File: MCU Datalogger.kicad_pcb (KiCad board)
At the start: 2 copper layers, 50.8 x 31.9 mm, 30 parts, among them J1 Conn_01x04_Pin, J2 Conn_01x04_Pin, J3 Conn_01x09_Pin, J4 Conn_02x03_Odd_Even, U1 24LC1025, U2 24LC1025, U3 ATMEGA328P-AU, U4 DS1337S_, Y1 32.768kHz, Y2 16KHz

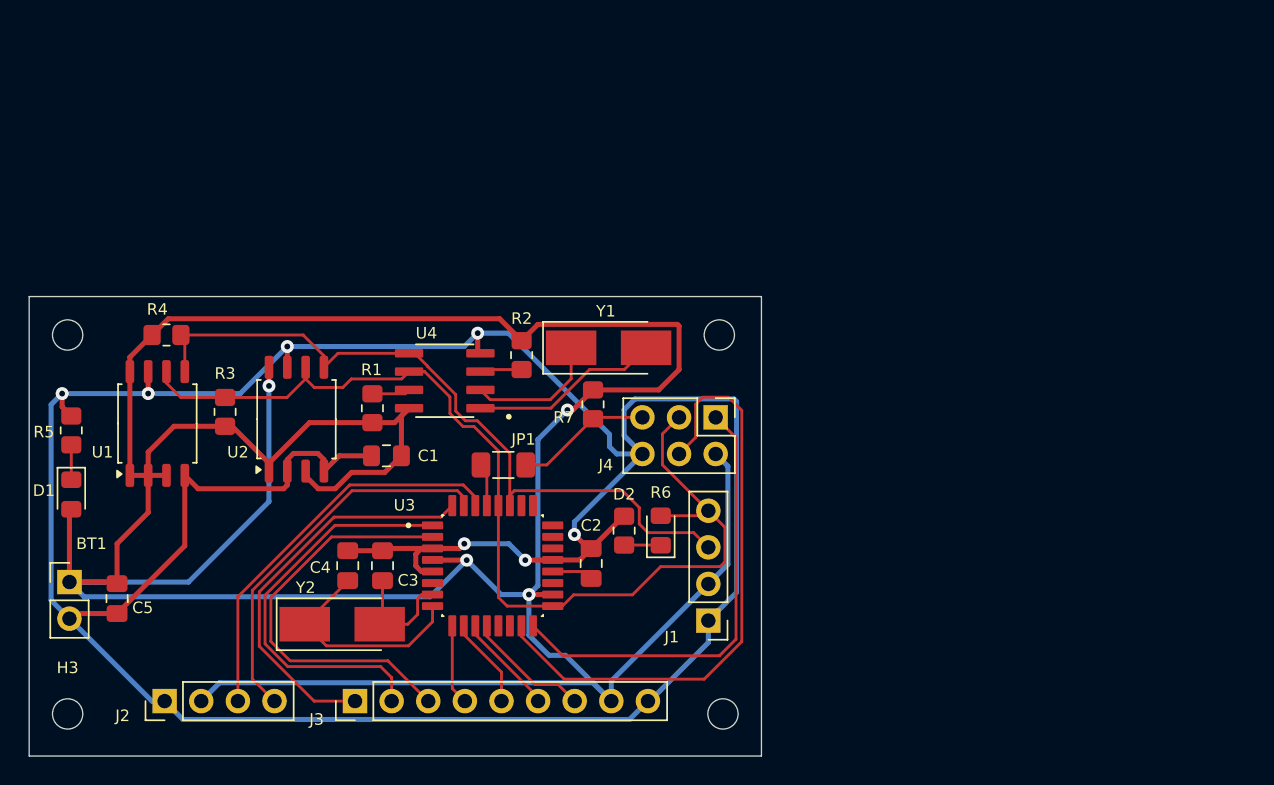
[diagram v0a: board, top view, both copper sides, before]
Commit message: fixed some issues with the EEPROM footprint 3d models
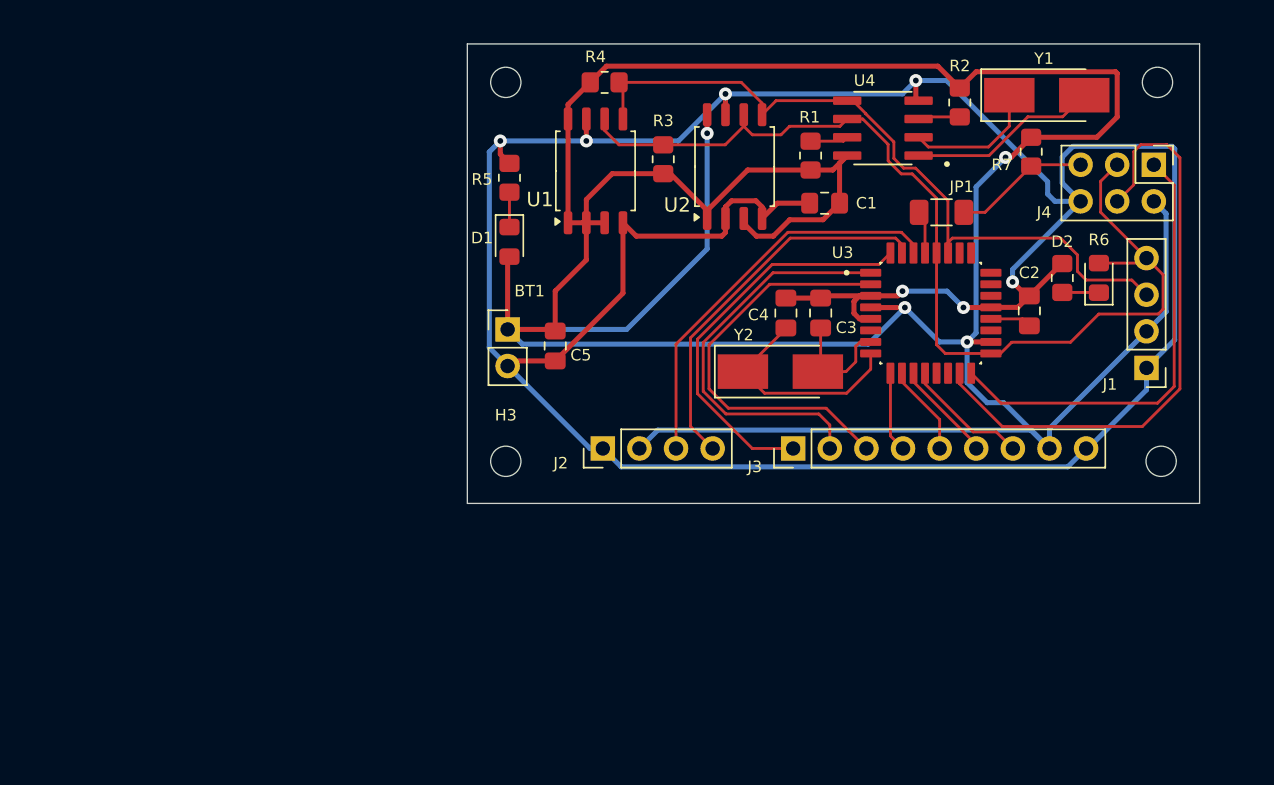
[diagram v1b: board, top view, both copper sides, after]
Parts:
- U1, U2: footprint Package_SO:SOIC-8_5.23x5.23mm_P1.27mm -> Package_SO:SOIC-8_5.275x5.275mm_P1.27mm
- moved BT1 35.1 mm to (118.0, 102.1)
- moved U1 35.1 mm to (124.1, 91.1)
- moved C2 35.1 mm to (154.2, 100.8)
- moved C3 35.1 mm to (139.7, 101.0)
- moved H1 35.1 mm to (117.9, 85.0)
- moved H2 35.1 mm to (163.1, 85.0)
- moved J2 35.1 mm to (124.6, 110.4)
- moved J3 35.1 mm to (137.8, 110.4)
- moved JP1 35.1 mm to (148.1, 94.0)
- moved R1 35.1 mm to (139.0, 90.0)
- moved R3 35.1 mm to (128.8, 90.3)
- moved R4 35.1 mm to (124.8, 85.0)
- moved R6 35.1 mm to (156.5, 98.5)
- moved R7 35.1 mm to (154.4, 89.8)
- moved U2 35.1 mm to (133.8, 90.8)
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
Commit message: finished the 2 layer PCB project
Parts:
- added REF**: ESD-Logo_6.6x6mm_SilkScreen, Symbol:ESD-Logo_6.6x6mm_SilkScreen, B.Cu at (137.0, 95.4)
- added REF**: KiCad-Logo2_5mm_SilkScreen, Symbol:KiCad-Logo2_5mm_SilkScreen, B.Cu at (142.1, 88.0)
- moved R5 13.0 mm to (125.3, 102.4)
- moved D1 7.83 mm to (122.9, 102.2), turned to 90 degrees
- moved R7 5.26 mm to (149.1, 89.5)
- moved Y1 3.65 mm to (152.1, 87.4), turned to -90 degrees
- moved J4 2.71 mm to (161.6, 88.3)
- moved C1 1.35 mm to (139.1, 92.3)
- moved C2 1.35 mm to (153.3, 99.8)
- moved C3 1.35 mm to (138.9, 99.9)
- moved D2 1.35 mm to (158.2, 97.5)
- moved J1 1.35 mm to (161.5, 103.8)
- moved J3 1.35 mm to (137.0, 109.3)
- moved JP1 1.35 mm to (147.2, 93.0)
- moved R1 1.35 mm to (138.2, 89.0)
- moved R6 1.35 mm to (155.6, 97.5)
- moved U2 1.35 mm to (132.9, 89.8)
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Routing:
- net /Vcc: track 254.1 -> 206.3 mm, vias 4 -> 5
- net GND: track 213.3 -> 237.3 mm, vias 7 -> 9
- net Net-(U4-X1): track 13.2 -> 6.92 mm
- net /RESET: track 9.07 -> 13.2 mm
- net /MISO: track 31.4 -> 28.6 mm
- net /MOSI: track 42.1 -> 40.1 mm
- net Net-(U4-X2): track 9.32 -> 7.70 mm
- net /SCK: track 72.4 -> 73.9 mm
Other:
- board size 50.8 x 31.9 mm -> 52.2 x 31.9 mm
- board text added: "2"
- board text added: "3"
- board text added: "4"
- board text added: "5"
- board text added: "6"
- board text added: "7"
- board text added: "8"
- board text added: "GND"
- board text added: "MISO"
- board text added: "MOSI"
- board text added: "RES"
- board text added: "RX"
- board text added: "SCK"
- board text added: "SDA"
- board text added: "TX"
- board text added: "VCC"
- board text added: "ver 1.0"

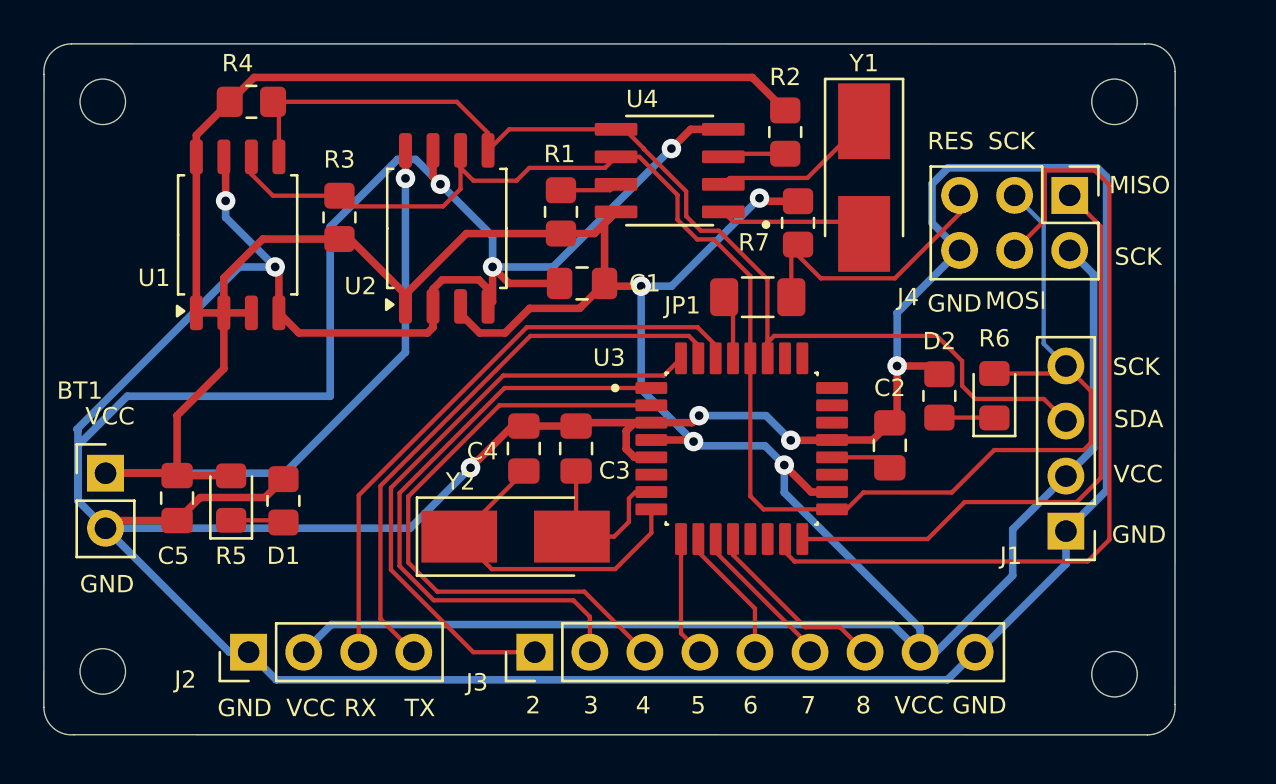
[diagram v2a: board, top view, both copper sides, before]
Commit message: modified routing and added a ground plane to the board
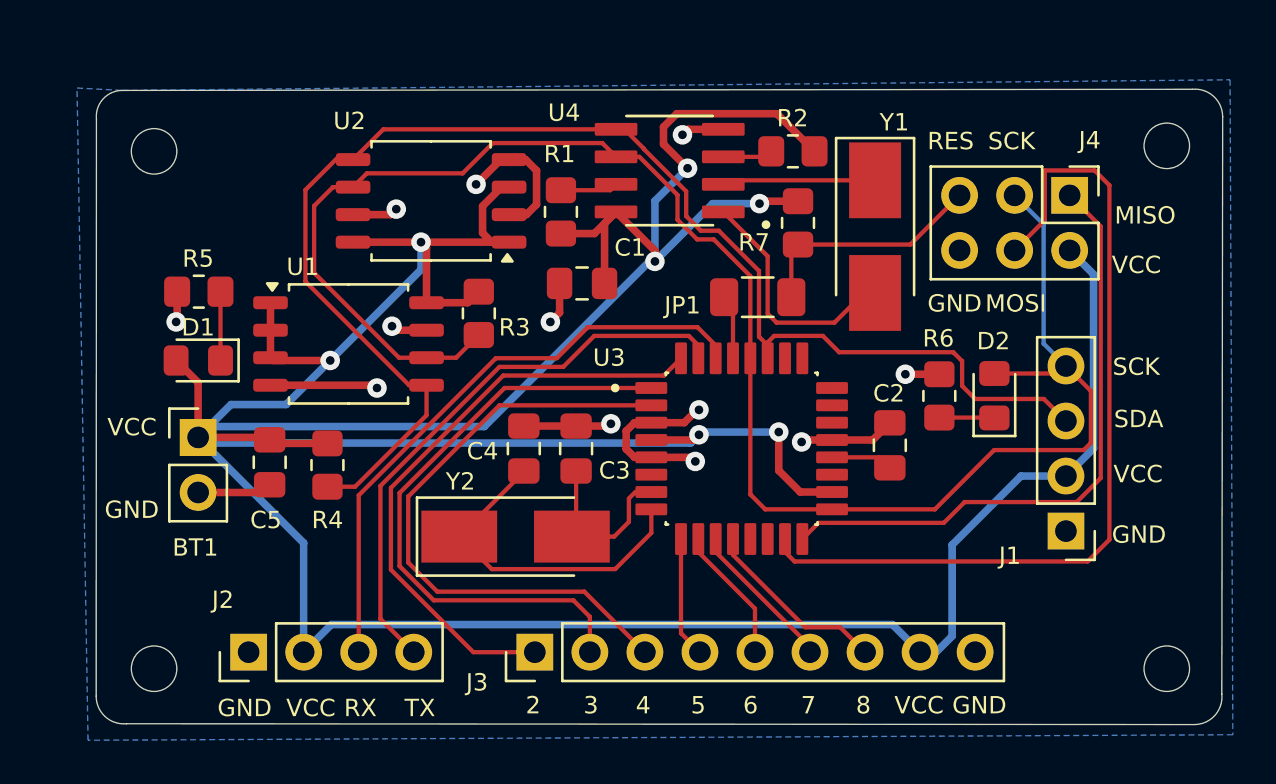
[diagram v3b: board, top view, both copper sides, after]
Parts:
- moved R4 17.1 mm to (127.4, 100.7), turned to 90 degrees
- moved R5 10.4 mm to (121.4, 92.7), turned to 180 degrees
- moved R3 7.81 mm to (134.4, 93.7), turned to -90 degrees
- moved U1 7.18 mm to (128.4, 95.1), turned to 0 degrees
- moved D1 6.53 mm to (121.4, 95.9), turned to 180 degrees
- moved BT1 4.58 mm to (121.4, 99.4)
- moved C5 4.58 mm to (124.7, 100.6)
- moved H1 3.29 mm to (119.4, 86.2)
- moved H2 3.15 mm to (166.1, 86.0)
- moved Y1 2.77 mm to (152.7, 90.2)
- moved H4 2.43 mm to (166.1, 110.1)
- moved H3 2.37 mm to (119.4, 110.1)
- moved U2 1.46 mm to (132.2, 88.5), turned to 180 degrees
- moved R2 0.96 mm to (148.9, 86.2), turned to 180 degrees
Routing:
- net GND: track 237.3 -> 42.1 mm, vias 9 -> 12
- net /SDA: track 51.4 -> 65.7 mm
- net /SCK: track 73.9 -> 81.0 mm
- net Net-(U4-X1): track 6.92 -> 10.7 mm
- net /Vcc: track 206.3 -> 203.5 mm, vias 5 -> 7
- net /RESET: track 13.2 -> 11.0 mm
- net Net-(U4-X2): track 7.70 -> 6.57 mm
- net Net-(D1-K): track 2.46 -> 3.18 mm
- net Net-(U4-~{INTA}): track 2.92 -> 2.32 mm
- added copper zone on B.Cu, net GND
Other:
- board size 52.2 x 31.9 mm -> 52 x 29.3 mm

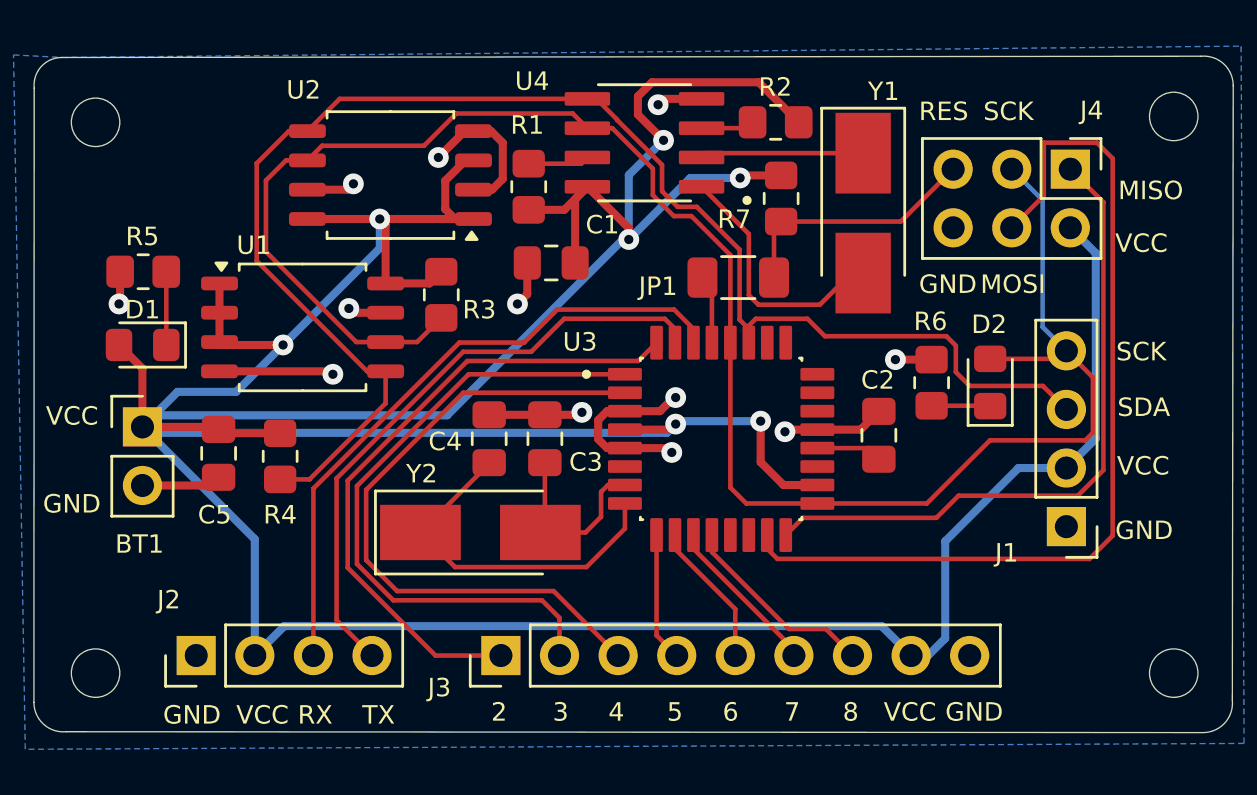
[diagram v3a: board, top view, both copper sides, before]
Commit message: finished routing the fixes to the 2 layer PCB
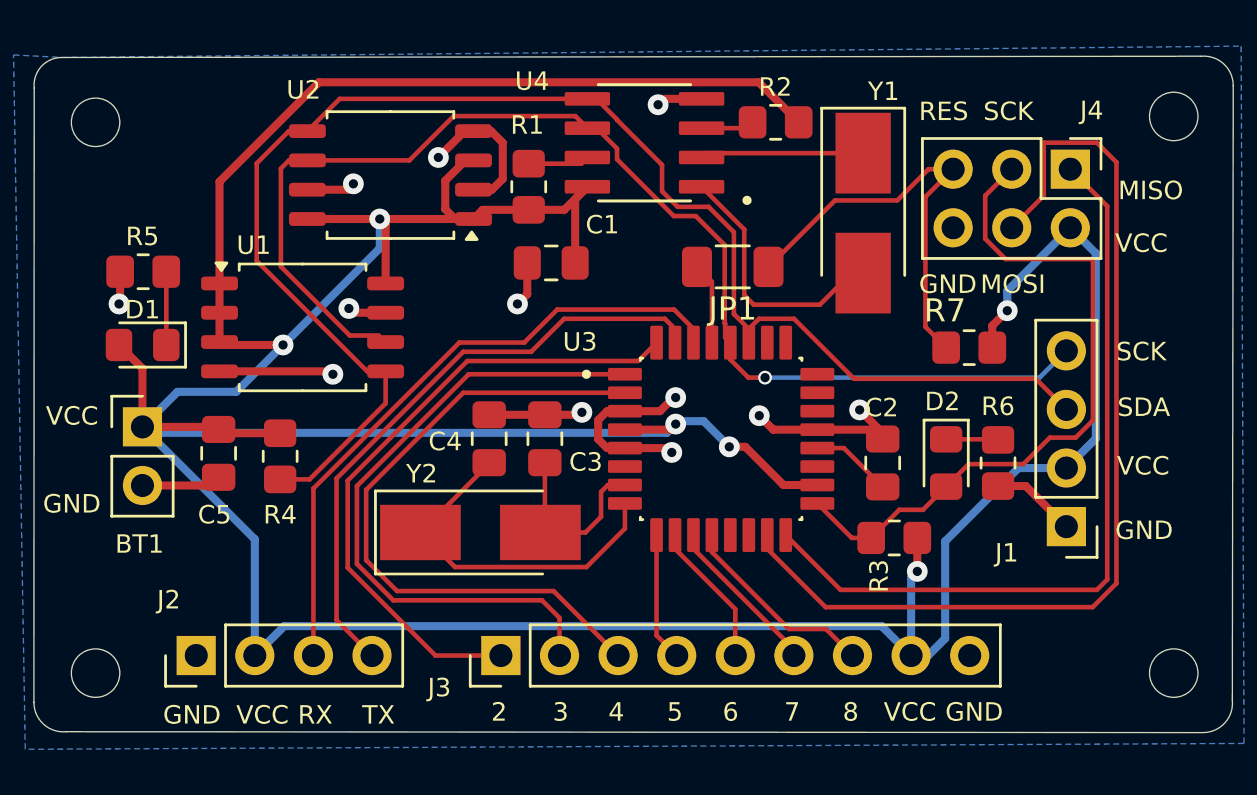
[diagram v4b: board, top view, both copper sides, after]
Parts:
- moved R3 22.3 mm to (154.0, 104.2), turned to 180 degrees
- moved R7 10.4 mm to (157.2, 96.0), turned to 0 degrees
- moved R6 4.52 mm to (158.5, 101.0), turned to 90 degrees
- moved D2 3.98 mm to (156.2, 101.0), turned to -90 degrees
- moved C2 1.21 mm to (153.5, 101.0)
- moved JP1 0.52 mm to (147.0, 92.5), turned to 180 degrees
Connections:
- J1 pad 4: /SCK -> /SCL
- JP1 pad 1: /RESET(JMP) -> /RESET
- JP1 pad 2: /RESET -> /RESET_JMP
- U1 pad 6: /SCK -> /SCL
- U2 pad 6: /SCK -> /SCL
- U3 pad 28: /SCK -> /SCL
- U3 pad 29: /RESET(JMP) -> /RESET_JMP
- U4 pad 6: /SCK -> /SCL
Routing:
- net /SCL: track 0.00 -> 52.6 mm, vias 0 -> 1
- net /SCK: track 81.0 -> 30.2 mm
- net /Vcc: track 203.5 -> 195.8 mm, vias 7 -> 6
- net /RESET: track 11.0 -> 18.4 mm
- net GND: track 42.1 -> 47.3 mm
- net /MISO: track 28.6 -> 33.6 mm
- net /RESET_JMP: track 0.00 -> 3.55 mm
- net /MOSI: track 40.1 -> 43.2 mm
- net /RESET(JMP): track 2.99 -> 0.00 mm
- net /SDA: track 65.7 -> 64.7 mm
- net Net-(U3-AREF): track 2.87 -> 3.53 mm
